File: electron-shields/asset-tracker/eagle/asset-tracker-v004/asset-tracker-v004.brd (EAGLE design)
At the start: 103 x 36 mm, 30 parts, among them J1 1X2-3.5MM, T1 DMG3415, U1 MAX-M8, U2 MAX2674, U3 LIS3DHTR, X1 ELECTRON, X2 IPEX-20279-001E

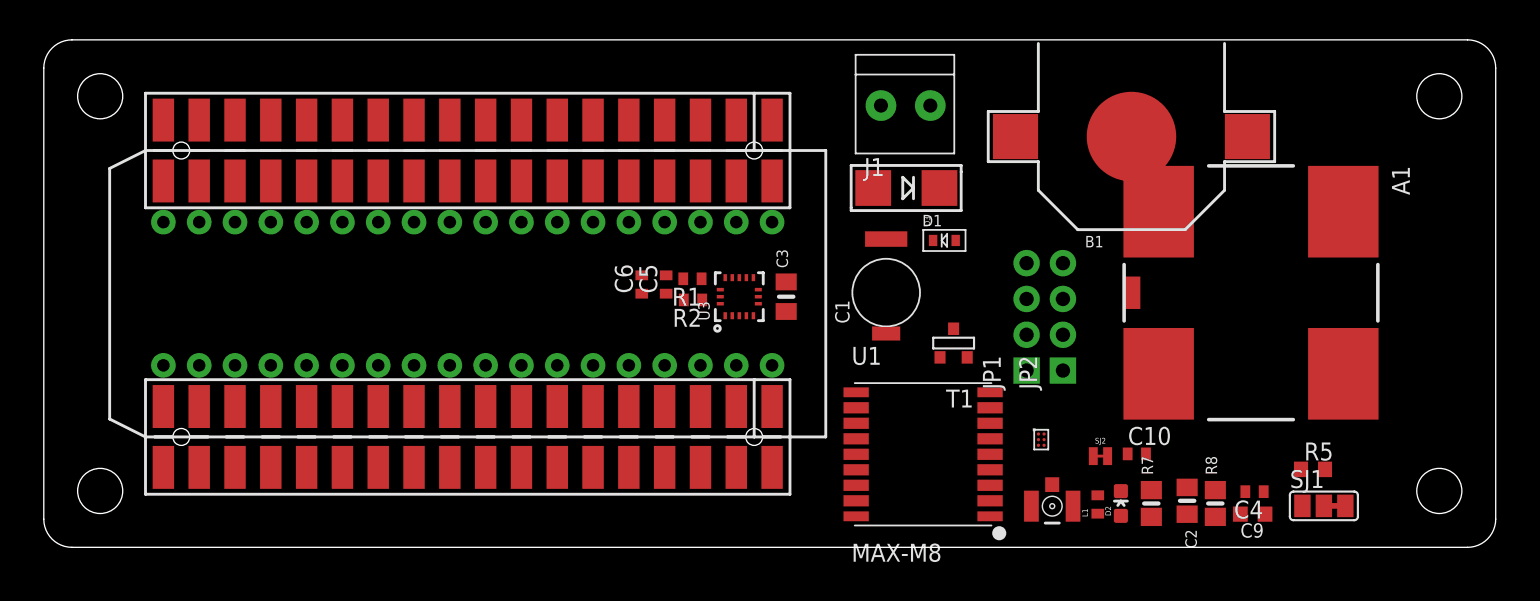
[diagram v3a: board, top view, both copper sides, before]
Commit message: added saw filter, li ion cell and routing almost complete
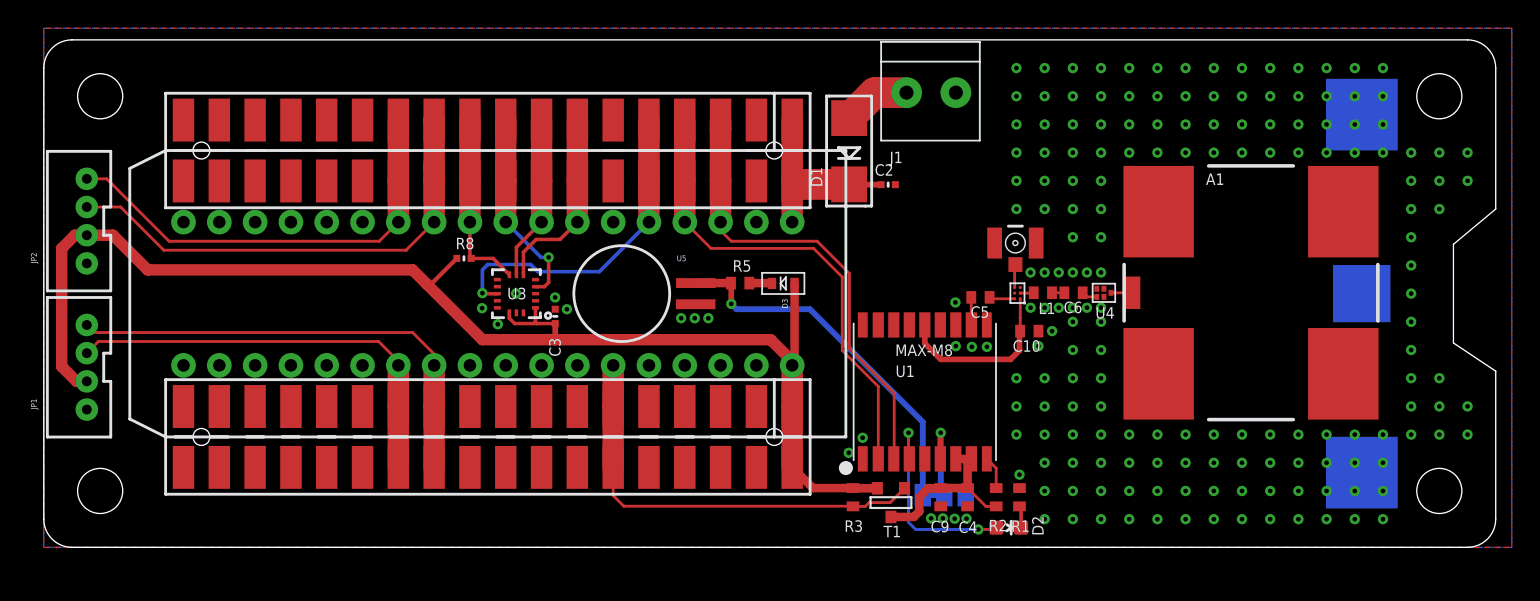
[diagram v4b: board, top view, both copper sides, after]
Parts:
- removed B1: CR1220, microbuilder:CR1220
- removed C1: 60mF, adafruit:414-VA5R
- removed R7: 10K, microbuilder:0805-NO
- removed SJ2: JUMPER-PAD-2-NC_BY_TRACENO_SILK, SparkFun-Passives:PAD-JUMPER-2-NC_BY_TRACE_NO_SILK
- added R3: 10K, rcl:R0402
- added U$26: (no value), adafruit:CR2032-SMD
- added U4: EPCOS-B9444, filters:QCS5I
- added U5: MS621FE, Explore Labs EAGLE Library:MS621FE
- C2: device microbuilder:0805-NO@1 -> microbuilder:_0402MP
- C3: device microbuilder:0805_10MGAP -> microbuilder:_0402MP
- C9: device rcl:C0603K -> rcl:C0402
- JP1, JP2: device SparkFun-Connectors:1X04_NO_SILK -> SparkFun-Connectors:JST-4-PTH-VERT
- R1: value (none) -> 1K
- R5: value 270 -> 1K; device rcl:R0603 -> rcl:R0402
- R8: device microbuilder:0805-NO -> microbuilder:_0402MP
- moved JP2 70.6 mm to (2.50, 23.1)
- moved JP1 67.2 mm to (2.50, 12.8)
- moved R8 56.1 mm to (29.8, 20.5), turned to 180 degrees
- moved R5 42.7 mm to (49.4, 18.7)
- moved C2 30.9 mm to (59.9, 25.7), turned to 0 degrees
- moved C6 30.6 mm to (73.0, 18.1), turned to 180 degrees
- moved R1 27.9 mm to (69.2, 3.56), turned to 270 degrees
- moved SJ1 26.9 mm to (63.9, 3.70), flipped to the bottom
- moved R2 25.7 mm to (67.6, 3.56), turned to 270 degrees
- moved C5 22.3 mm to (66.4, 17.7), turned to 180 degrees
- moved C9 22.2 mm to (63.6, 3.56), turned to 90 degrees
- moved C4 20.4 mm to (65.5, 3.56), turned to 90 degrees
- moved X2 18.8 mm to (68.9, 21.6), turned to 180 degrees
- moved C3 16.4 mm to (36.3, 16.4)
- moved U3 15.8 mm to (33.5, 18.0), turned to 180 degrees
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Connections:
- net 3.3V: now also D3.A, JP1.2, JP2.2, R3.2; no longer JP1.3, JP2.3, R7.2, SJ2.2
- net A0: now also JP2.4; no longer JP1.1
- net A1: now also JP2.3; no longer JP1.2
- net GND: now also J1.2, JP1.1, JP2.1, U$26.+$1, U$26.+$2, U4.2, U4.3, U4.5, U5.NEG; no longer B1.-, C1.-, J1.1, JP1.4, JP2.4
- net GPS_PWR_EN: now also R3.1; no longer R7.1
- net N$1: now also C6.1, U4.4; no longer D3.A, SJ2.1
- net N$11: now also U$26.-; no longer B1.+$1
- net N$12: now also U4.1; no longer C6.1
- net N$7: now also U5.POS; no longer C1.+
- net N$9: now also J1.1; no longer J1.2
- net SCL: now also JP1.4; no longer JP2.1
- net SDA: now also JP1.3; no longer JP2.2
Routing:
- net 3.3V: track 0.00 -> 95.5 mm
- net GPS_TXD: track 0.00 -> 34.0 mm
- net A1: track 0.00 -> 34.0 mm
- net SCL: track 0.00 -> 33.5 mm
- net GPS_RXD: track 0.00 -> 32.7 mm
- net A0: track 0.00 -> 31.7 mm
- net GPS_PWR_EN: track 0.00 -> 30.8 mm
- net SDA: track 0.00 -> 30.6 mm
- net N$7: track 0.00 -> 26.2 mm, vias 0 -> 1
- net ACCEL_INT1: track 0.00 -> 23.6 mm, vias 0 -> 1
- net TIMEPULSE: track 0.00 -> 14.7 mm, vias 0 -> 2
- net ACCEL_SCK: track 0.00 -> 14.2 mm, vias 0 -> 1
- net N$8: track 0.00 -> 13.7 mm
- net ACCEL_MOSI: track 0.00 -> 13.5 mm
- net ACCEL_CS: track 0.00 -> 13.0 mm
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- added copper zone on layer 1, net GND
- added copper zone on layer 16, net GND
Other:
- outline, holes or cut-outs redrawn
- board text added: "ANTENNA"
- board text added: "BATTERY"
